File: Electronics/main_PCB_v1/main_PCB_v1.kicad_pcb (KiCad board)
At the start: 4 copper layers, 117.4 x 80.5 mm, 156 parts, among them IC202 TJA1057GT/3, IC203 TJA1057GT/3, J201 MEM2075-00-140-01-A, J203 TYPE-C-31-M-12, J204 Conn_02x04_Odd_Even, J205 Conn_ST_STDC14, J207 Conn_01x04, J208 SM02B-GHS-TB_LF__SN_, J209 SM02B-GHS-TB_LF__SN_, J210 SM02B-GHS-TB_LF__SN_, J211 SM02B-GHS-TB_LF__SN_, J212 SM02B-GHS-TB_LF__SN_, J301 Conn_01x02, J305 Conn_01x02, J306 Conn_01x02, J307 Conn_01x02, J308 Conn_01x02, J309 Conn_01x02, J310 Conn_01x02, J401 Conn_Coaxial, Q302 DMP3028LFDE, T301 NVMFS4C05NT1G, T302 NVMFS4C05NT1G, U201 STM32H723ZGT6, U202 USBLC6-4SC6, U203 USBLC6-4SC6, U204 BMI270, U206 LIS3MDL, U211 M24C08-FMH6TG, U301 LMR43620MB5RPER, U302 LMR43620MB5RPER, U401 NRF24L01, U402 RFX2401C, X201 25MHz_Clock, X202 32.768kHz_Clock, Y402 16M

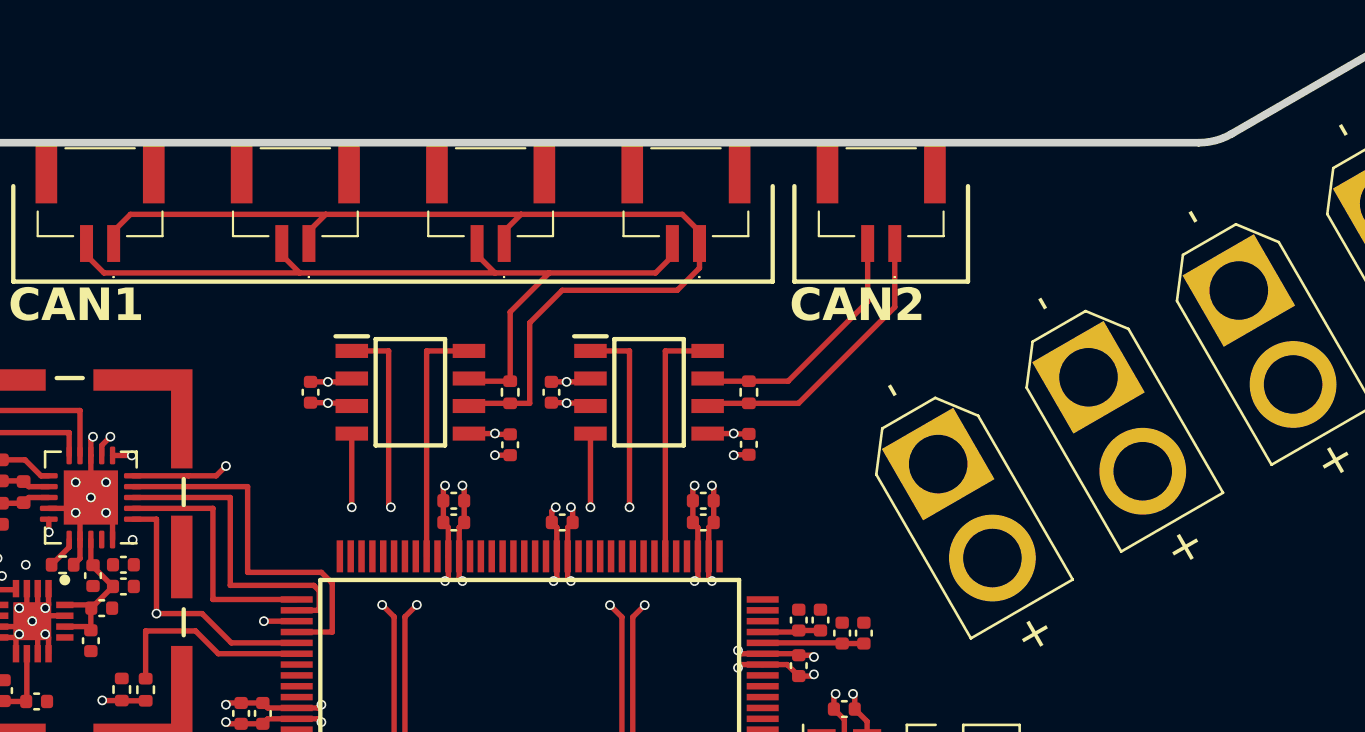
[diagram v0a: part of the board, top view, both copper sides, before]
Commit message: Added 12V rail to PCB
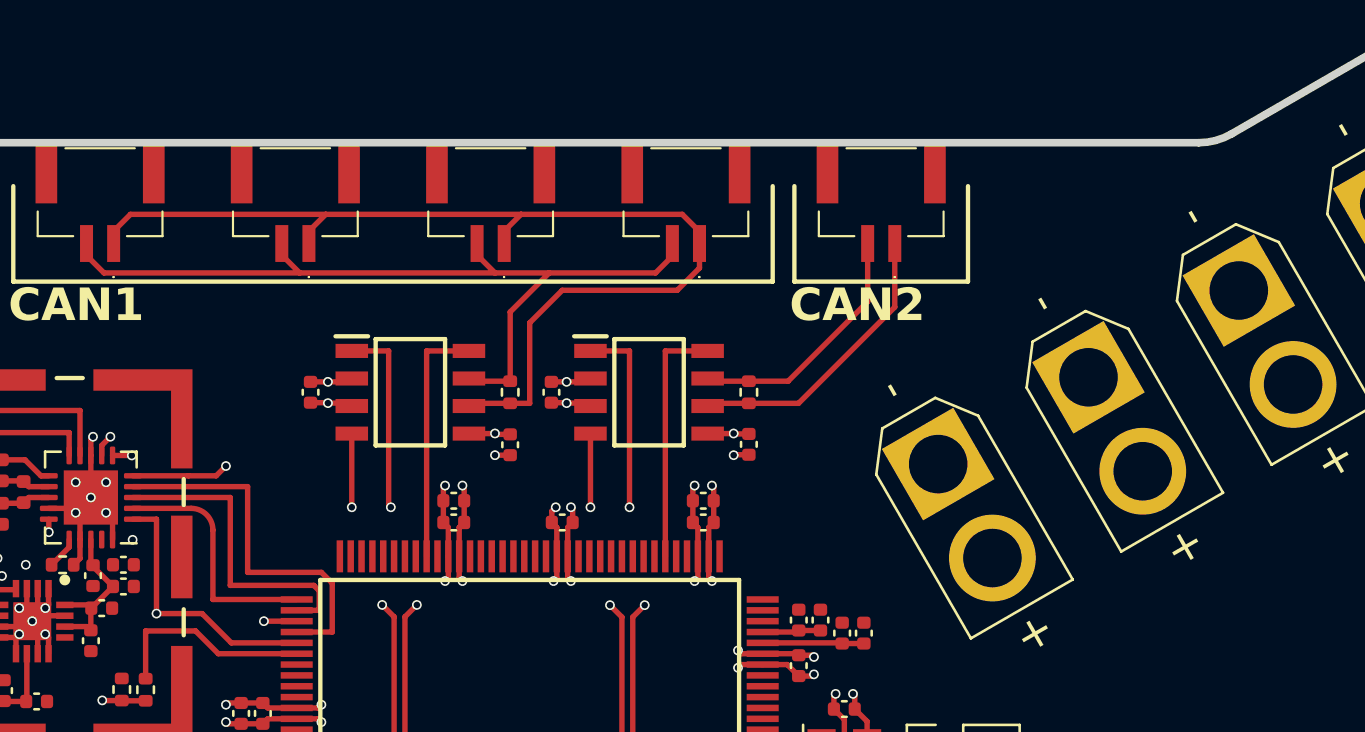
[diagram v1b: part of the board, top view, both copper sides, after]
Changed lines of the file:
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@@
     (fp_arc (start -4 44.928847) (mid -4.952925 46.632831) (end -6.903614 46.713078)
       (stroke (width 2) (type solid)) (layer "B.Mask"))
-    (fp_arc (start 32.682975 -10) (mid 31.647701 -10.136298) (end 30.682975 -10.535898)
+    (fp_arc (start 32.682975 -10) (mid 31.647699 -10.1363) (end 30.682975 -10.535898)
       (stroke (width 2) (type solid)) (layer "B.Mask"))
-    (fp_arc (start 51 -10) (mid 52.414228 -9.414228) (end 53 -8)
+    (fp_arc (start 51 -10) (mid 52.414213 -9.414214) (end 53 -8)
       (stroke (width 2) (type solid)) (layer "B.Mask"))
-    (fp_arc (start 53 33.883253) (mid 52.414217 35.297485) (end 51 35.883253)
+    (fp_arc (start 53 33.883253) (mid 52.41423 35.297497) (end 51 35.883253)
       (stroke (width 2) (type solid)) (layer "B.Mask"))
     (fp_poly
@@
     (fp_arc (start -43.896309 -4.235489) (mid -44.701842 -4.972842) (end -45 -6.023401)
       (stroke (width 2) (type solid)) (layer "F.Mask"))
-    (fp_arc (start -43.896309 -4.235489) (mid -41.155989 -0.200281) (end -43.156129 4.248506)
+    (fp_arc (start -43.896309 -4.235489) (mid -41.155989 -0.20028) (end -43.156129 4.248506)
       (stroke (width 2) (type solid)) (layer "F.Mask"))
     (fp_arc (start -6.903614 46.713078) (mid -28.612293 30.979111) (end -44.340324 9.266131)
@@
     (fp_arc (start -4 44.928847) (mid -4.952925 46.632831) (end -6.903614 46.713078)
       (stroke (width 2) (type solid)) (layer "F.Mask"))
-    (fp_arc (start 32.682975 -10) (mid 31.647701 -10.136298) (end 30.682975 -10.535898)
+    (fp_arc (start 32.682975 -10) (mid 31.647699 -10.1363) (end 30.682975 -10.535898)
       (stroke (width 2) (type solid)) (layer "F.Mask"))
-    (fp_arc (start 51 -10) (mid 52.414224 -9.414227) (end 53 -8)
+    (fp_arc (start 51 -10) (mid 52.414213 -9.414214) (end 53 -8)
       (stroke (width 2) (type solid)) (layer "F.Mask"))
-    (fp_arc (start 53 33.883253) (mid 52.414211 35.297475) (end 51 35.883253)
+    (fp_arc (start 53 33.883253) (mid 52.414216 35.297467) (end 51 35.883253)
       (stroke (width 2) (type solid)) (layer "F.Mask"))
     (fp_poly
@@
     (fp_line (start 53.99132 -8) (end 53.99132 33.883252)
       (stroke (width 0.35) (type solid)) (layer "Edge.Cuts"))
-    (fp_arc (start -46.00868 -26.078963) (mid -45.906466 -26.855422) (end -45.606756 -27.578963)
+    (fp_arc (start -46.00868 -26.078963) (mid -45.906466 -26.855423) (end -45.606756 -27.578963)
       (stroke (width 0.35) (type solid)) (layer "Edge.Cuts"))
     (fp_arc (start -45.241243 9.717693) (mid -45.646335 6.311399) (end -43.761 3.445662)
@@
     (fp_arc (start -44.353144 -3.341534) (mid -45.561442 -4.447564) (end -46.00868 -6.023402)
       (stroke (width 0.35) (type solid)) (layer "Edge.Cuts"))
-    (fp_arc (start -44.353144 -3.341534) (mid -42.160897 -0.113366) (end -43.761 3.445662)
+    (fp_arc (start -44.353144 -3.341534) (mid -42.160897 -0.113367) (end -43.761 3.445662)
       (stroke (width 0.35) (type solid)) (layer "Edge.Cuts"))
-    (fp_arc (start -34.916356 -46.095278) (mid -33.094744 -47.49308) (end -30.81828 -47.193354)
+    (fp_arc (start -34.916356 -46.095278) (mid -33.094743 -47.49308) (end -30.81828 -47.193354)
       (stroke (width 0.35) (type solid)) (layer "Edge.Cuts"))
     (fp_arc (start -7.364102 47.605193) (mid -29.328177 31.68612) (end -45.241243 9.717693)
@@
     (fp_arc (start -3.00868 39.883252) (mid -2.129988 37.761944) (end -0.00868 36.883252)
       (stroke (width 0.35) (type solid)) (layer "Edge.Cuts"))
-    (fp_arc (start -3.00868 44.928846) (mid -4.438041 47.484867) (end -7.364102 47.605193)
+    (fp_arc (start -3.00868 44.928846) (mid -4.43804 47.484867) (end -7.364102 47.605193)
       (stroke (width 0.35) (type solid)) (layer "Edge.Cuts"))
-    (fp_arc (start 32.674296 -11) (mid 31.897836 -11.102219) (end 31.174296 -11.401924)
+    (fp_arc (start 32.674296 -11) (mid 31.897841 -11.102227) (end 31.174296 -11.401924)
       (stroke (width 0.35) (type solid)) (layer "Edge.Cuts"))
-    (fp_arc (start 50.99132 -11) (mid 53.11267 -10.121345) (end 53.99132 -8)
+    (fp_arc (start 50.99132 -11) (mid 53.112657 -10.121342) (end 53.99132 -8)
       (stroke (width 0.35) (type solid)) (layer "Edge.Cuts"))
-    (fp_arc (start 53.99132 33.883252) (mid 53.112651 36.004581) (end 50.99132 36.883252)
+    (fp_arc (start 53.99132 33.883252) (mid 53.112652 36.004575) (end 50.99132 36.883252)
       (stroke (width 0.35) (type solid)) (layer "Edge.Cuts"))
     (fp_circle (center -30.75035 25.792588) (end -27.70035 25.792588)
@@
   (segment (start 130.8 96.2) (end 130.75 96.25) (width 0.25) (layer "F.Cu") (net 177))
   (segment (start 130.8 95.3505) (end 130.8 96.2) (width 0.25) (layer "F.Cu") (net 177))
-  (segment (start 125.9 91.55) (end 125.9 95.75) (width 0.25) (layer "F.Cu") (net 178))
-  (segment (start 122.2125 91.55) (end 125.9 91.55) (width 0.25) (layer "F.Cu") (net 178))
+  (segment (start 125.9 92.55) (end 125.9 95.75) (width 0.25) (layer "F.Cu") (net 178))
+  (segment (start 122.2125 91.55) (end 124.9 91.55) (width 0.25) (layer "F.Cu") (net 178))
   (segment (start 125.9 95.75) (end 129.762 95.75) (width 0.25) (layer "F.Cu") (net 178))
+  (arc (start 125.9 92.55) (mid 125.607107 91.842893) (end 124.9 91.55) (width 0.25) (layer "F.Cu") (net 178))
   (segment (start 124 107.75) (end 124 107.5) (width 0.25) (layer "F.Cu") (net 185))
   (segment (start 121.067107 108.957107) (end 120.31 108.2) (width 0.25) (layer "F.Cu") (net 185))
